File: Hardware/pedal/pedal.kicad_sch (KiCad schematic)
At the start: 34 parts, among them J101 USB_C_Receptacle_USB2.0_16P, J102 Barrel_Jack_Switch, J103 AudioJack3_SwitchTR, SW101 SW_SPST, SW102 RotaryEncoder_Switch_MP, U101 USBLC6-2P6, U102 TPS62153, U103 TLV76733DRVx

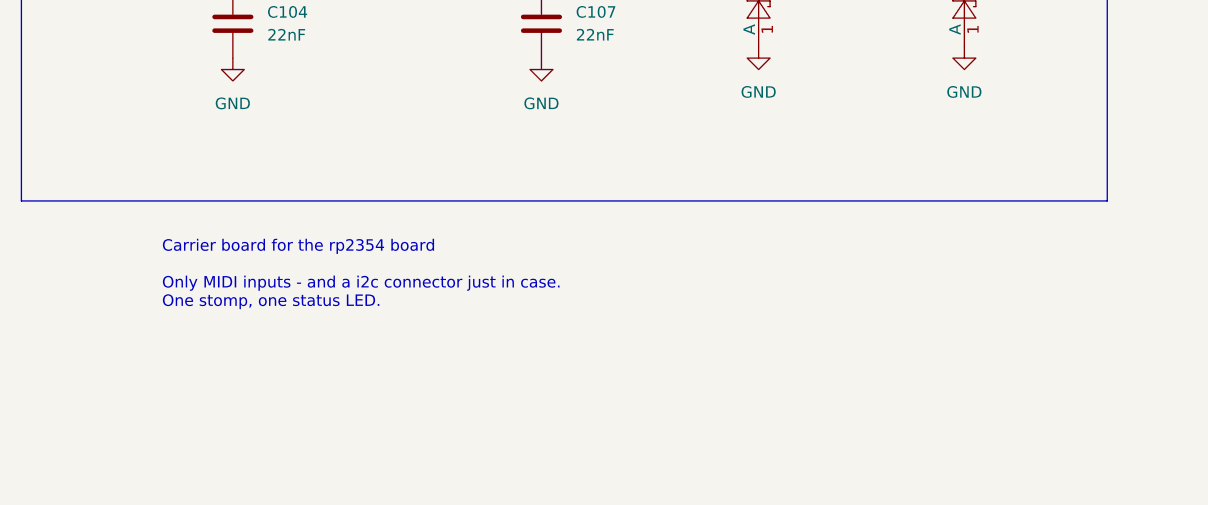
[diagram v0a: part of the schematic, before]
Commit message: Rename the guitar pedal hardware design files
The 'usb-stomp' name is entirely historical, from when this was just the
board with a stomp switch and a USB connector, and connectors for the
RP2354 MCU board and to the audio jacks.

Now it's the whole pedal. So name it that.

This also gets rid of the design block remnants in the schematic.  I'd
still like to have the notion of a design block, but not the way kicad
does it.  It was a valiant attempt, it just didn't work out.

Signed-off-by: Linus Torvalds <torvalds@linux-foundation.org>
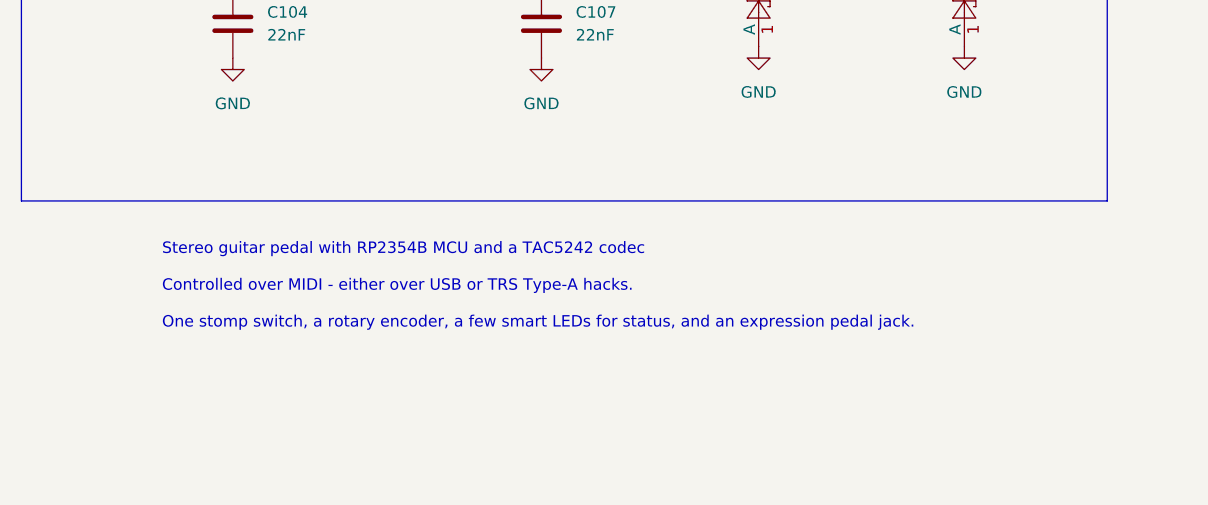
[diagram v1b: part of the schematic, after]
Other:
- note added: "Stereo guitar pedal with RP2354B MCU and a TAC5242 codec Controlled over MIDI - either over USB or TRS Type-A hacks. One stomp switch, a rotary encoder, a few smart LEDs for status, and an expression pedal jack."
- note removed: "Carrier board for the rp2354 board Only MIDI inputs - and a i2c connector just in case. One stomp, one status LED."

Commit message: Create a new board version with 8MB PSRAM and dual stomp switches
This adds a 8MB of external memory to the RP2354.  It's worth noting
that such memory is much slower than the internal SRAM, so while the
intended use is very much for audio effects to store more audio state
(for a looper or a longer echo), it needs to be treated carefully.

The PSRAM _can_ be accessed as just regular memory, exactly the same way
the flash works (it's all using the same QSPI interface).

But the preferred model will be to use a DMA engine to move the data
asynchronously between the on-die SRAM and the off-chip PSRAM, so that
the audio engine running on core 1 will not see random delay states from
the QSPI accesses.

The second stomp switch is partly to make it easier to control any
looper interface, but partly because this pedal really did want two
stomp switches for controlling: you might use one for bypass, and the
other to switch between scenes.

A remote stomp obviously would also work, but let's make really basic
functionality available on the pedal directly.

Note that this will also require a new board file: the GPIO mappings
have changed to make the PCB routing simpler.  I wanted to use GPIO0 for
the new PSRAM QSPI chip select line, because it's right there in that
corner of the RP2354A chip.  But we used to use it for the stomp switch.

And once I changed one GPIO mapping, I might as well change the others,
since a board update is a board update, and the old routing was odd for
historical reasons, going all the way back to how the i2s lines went
over the BM28 connectors and the FFC cable.

So now the GPIO mappings are

 GPIO0: PSRAM QSPI CS1n (didn't exist before)
 GPIO8/9: MIDI UART TX/RX (used to be  20/21)
 GPIO10/19: STOMP 0/1 (used to be GPIO0 for STOMP0)
 GPIO11: WS2812B chain (used to be GPIO25)
 GPIO12..14: rotary encoder A/B/SW (stays the same)
 GPIO20..23: i2s DIN/DOUT/FSYNC/BCLK (used to be 10/11/9/8)

 ADC0/1: expression pedal Tip and Ring (used to be other way ar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
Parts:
- removed D106: 1N5819WS, Diode_SMD:D_SOD-323, symbol Device:D_Schottky
- added D106: BAT54SW, Package_TO_SOT_SMD:SOT-323_SC-70, symbol Diode:BAT54SW
- added SW101: SW_SPST, Mylib:Daier PBS-24B-2, symbol Switch:SW_SPST
- renumbered C105 to C104, C104 to C105, C108 to C107, C107 to C108, R106 to R105, R105 to R106, SW101 to SW102, SW102 to SW103
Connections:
- net BOOTSEL: now also D106.3 (COM)
- net EXP_R: now also R106.2; no longer R104.2
- net EXP_T: now also R104.2; no longer R106.2
- net GND: now also SW102.1 (A), SW101.2 (B); no longer SW102.2 (B)
- net GPIO0: no longer SW102.1 (A)
- net GPIO10: now also SW102.2 (B)
- net GPIO19: now also SW101.1 (A)
- net at R107.1, SW103.S1: now also D106.2 (K)
- no-connect marks 19 -> 18
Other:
- note added: "Stereo guitar pedal with RP2354A MCU and a TAC5242 codec Controlled over MIDI - either over USB or TRS Type-A hacks. Two stomp switches, a rotary encoder, five smart LEDs for status, an expression pedal jack, and 8MB of QSPI PSRAM."
- note removed: "Stereo guitar pedal with RP2354B MCU and a TAC5242 codec Controlled over MIDI - either over USB or TRS Type-A hacks. One stomp switch, a rotary encoder, a few smart LEDs for status, and an expression pedal jack."
- moved on the sheet: C105, C108, D105, D107, J103, R104, R106, SW102

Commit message: Create a new rotary encoder footprint
The standard kicad footprint has long driven me mad.  It's centered on
pin 1, because of whatever insane reasons.  But the location of pin 1 on
a rotary is completely pointless and wrong: the only actual location
that matters is the location of the _shaft_ of the rotary.  That's the
one you want to place.

And this annoyance came to a head when the vendor 3D model I found is sane.

So the insane kicad footprint goes out the window, replaced by something
that actually makes sense.  And associated with a vendor 3D model with
the sensible placement too.

The pedal design has been updated and now the 3D view shows it in all
its proper glory.

Except for the stomp switch. Which I'm afraid I will have to model myself.

It's going to be ugly.  You have been warned.  And the ugliness is only
going to be accentuated by all the much prettier models that will
surround it.  Too bad.

Signed-off-by: Linus Torvalds <torvalds@linux-foundation.org>
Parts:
- SW103: footprint Rotary_Encoder:RotaryEncoder_Alps_EC11E-Switch_Vertical_H20mm -> Mylib:RotaryEncoder_EC11-Switch_Vertical_H20mm
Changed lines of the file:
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@@
 			)
 		)
-		(property "Footprint" "Rotary_Encoder:RotaryEncoder_Alps_EC11E-Switch_Vertical_H20mm"
+		(property "Footprint" "Mylib:RotaryEncoder_EC11-Switch_Vertical_H20mm"
 			(at 242.57 103.886 0)
 			(hide yes)
